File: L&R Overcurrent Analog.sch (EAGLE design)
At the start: 22 parts, among them IC1 CSLA2CFTH, IC2 TLC393CPN, IC3 7805TV, Q1 SUP75P0307, Q2 SUP75P0307, X1 J1

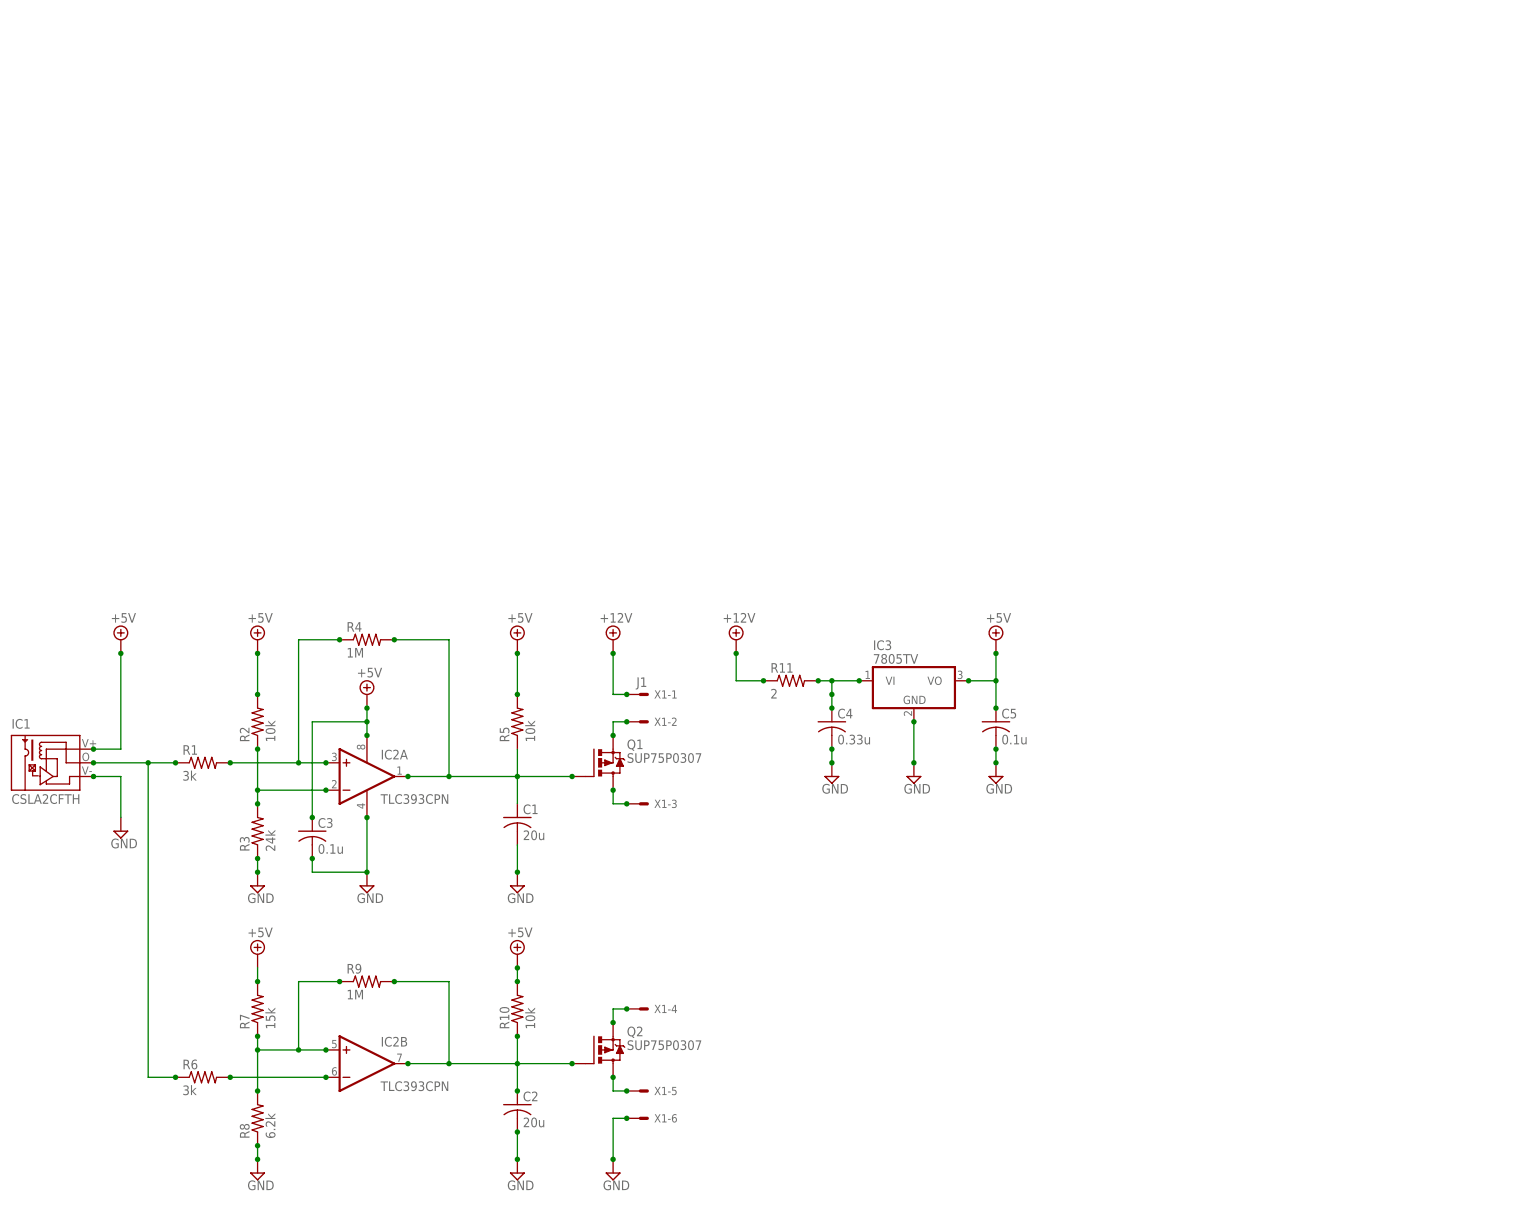
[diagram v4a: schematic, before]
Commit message: Split transducer from main board, added schematic frame.
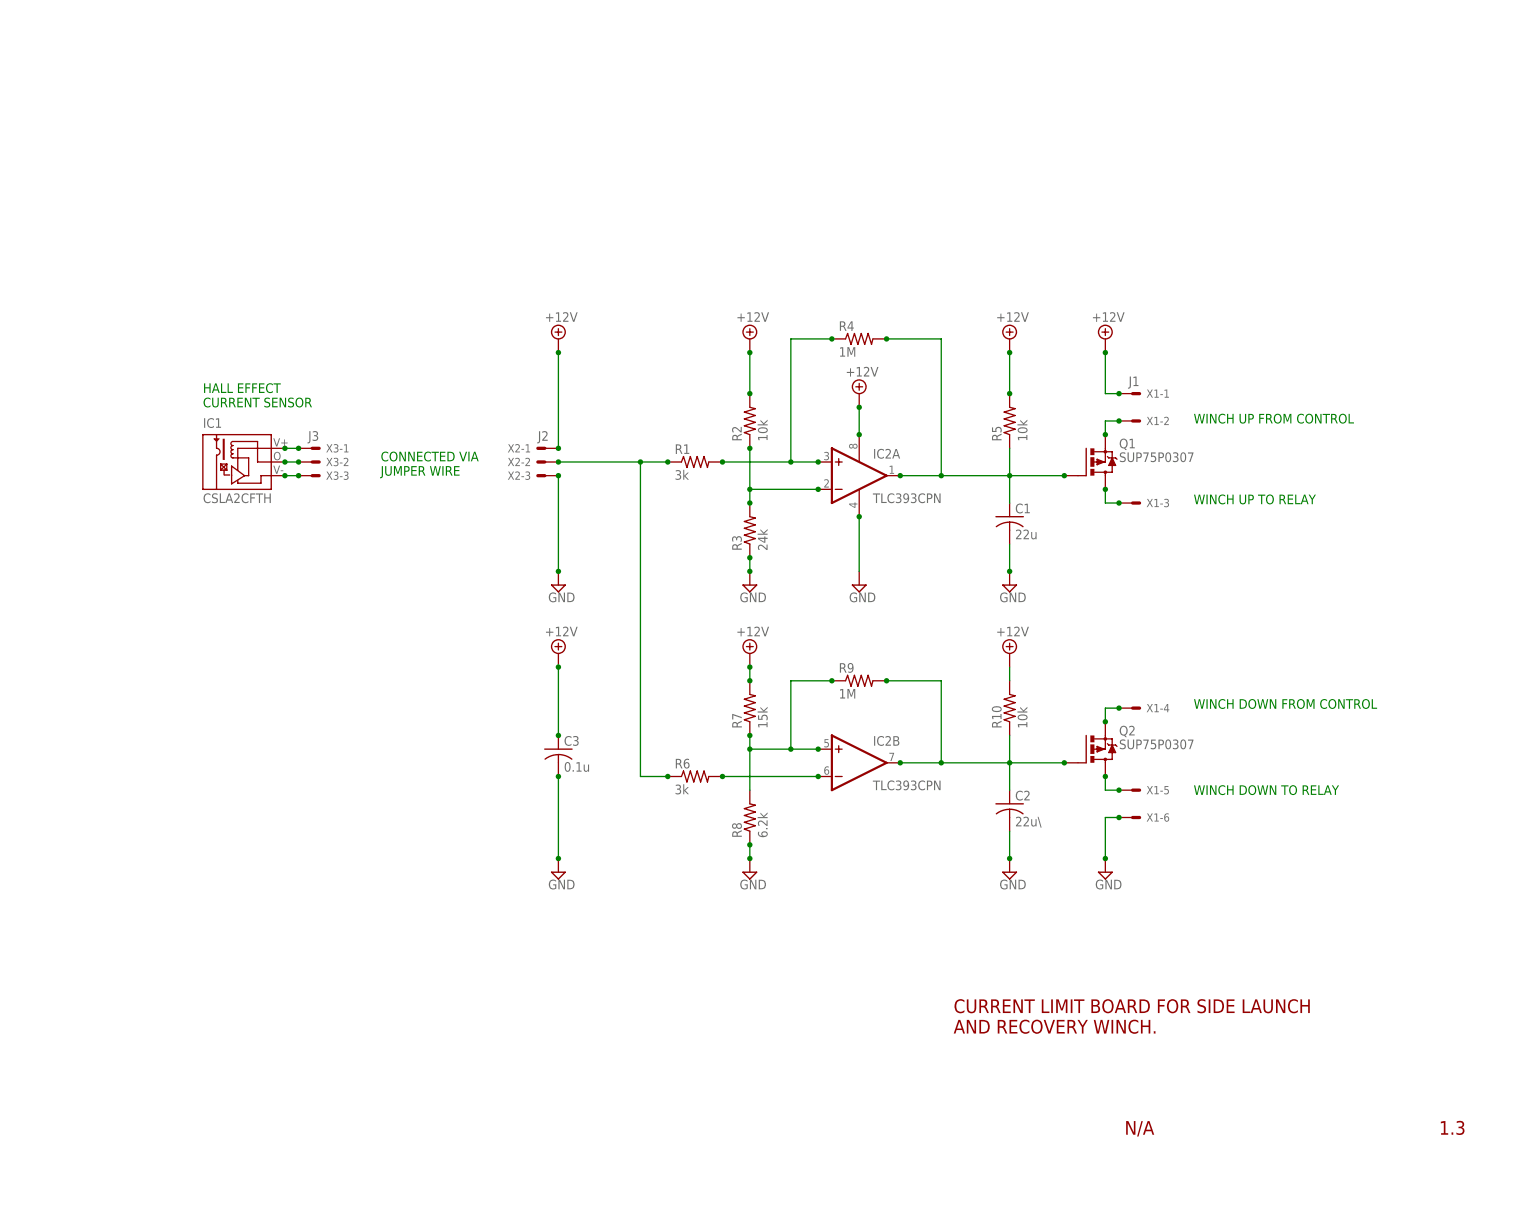
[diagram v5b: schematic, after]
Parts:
- removed C4: 0.33u, Overcurrent Detect:CAPACITOR-US
- removed C5: 0.1u, Overcurrent Detect:CAPACITOR-US
- removed IC3: 7805TV, Overcurrent Detect:7805TV
- removed R11: 2, Overcurrent Detect:RESISTOR-US0617/22
- added X2: J2, Overcurrent Detect:22-23-2031
- added X3: J3, Overcurrent Detect:22-23-2031
- C1: value 20u -> 22u
- C2: value 20u -> 22u\
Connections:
- removed net +5V: C3.1, C5.1, IC1.V+, IC2P.V+, IC3.VO, R10.2, R2.2, R5.2, R7.2
- removed net N$3: IC1.M, R1.1, R6.1
- new net N$13: IC1.V-, X3-3.S
- new net N$14: IC1.M, X3-2.S
- new net N$15: R1.1, R6.1, X2-2.S
- net +12V: now also C3.1, IC2P.V+, R10.2, R2.2, R5.2, R7.2, X2-1.S; no longer R11.1
- net GND: now also X2-3.S; no longer C4.2, C5.2, IC1.V-, IC3.GND
- net N$12: now also IC1.V+, X3-1.S; no longer C4.1, IC3.VI, R11.2
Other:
- note added: "1.3"
- note added: "CONNECTED VIA JUMPER WIRE"
- note added: "CURRENT LIMIT BOARD FOR SIDE LAUNCH AND RECOVERY WINCH."
- note added: "HALL EFFECT CURRENT SENSOR"
- note added: "N/A"
- note added: "WINCH DOWN FROM CONTROL"
- note added: "WINCH DOWN TO RELAY"
- note added: "WINCH UP FROM CONTROL"
- note added: "WINCH UP TO RELAY"
- moved on the sheet: C1, C2, C3, IC1, IC2A, IC2B, Q1, Q2, R1, R10, R2, R3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

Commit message: Updated / added document frames and added cutout to PCB
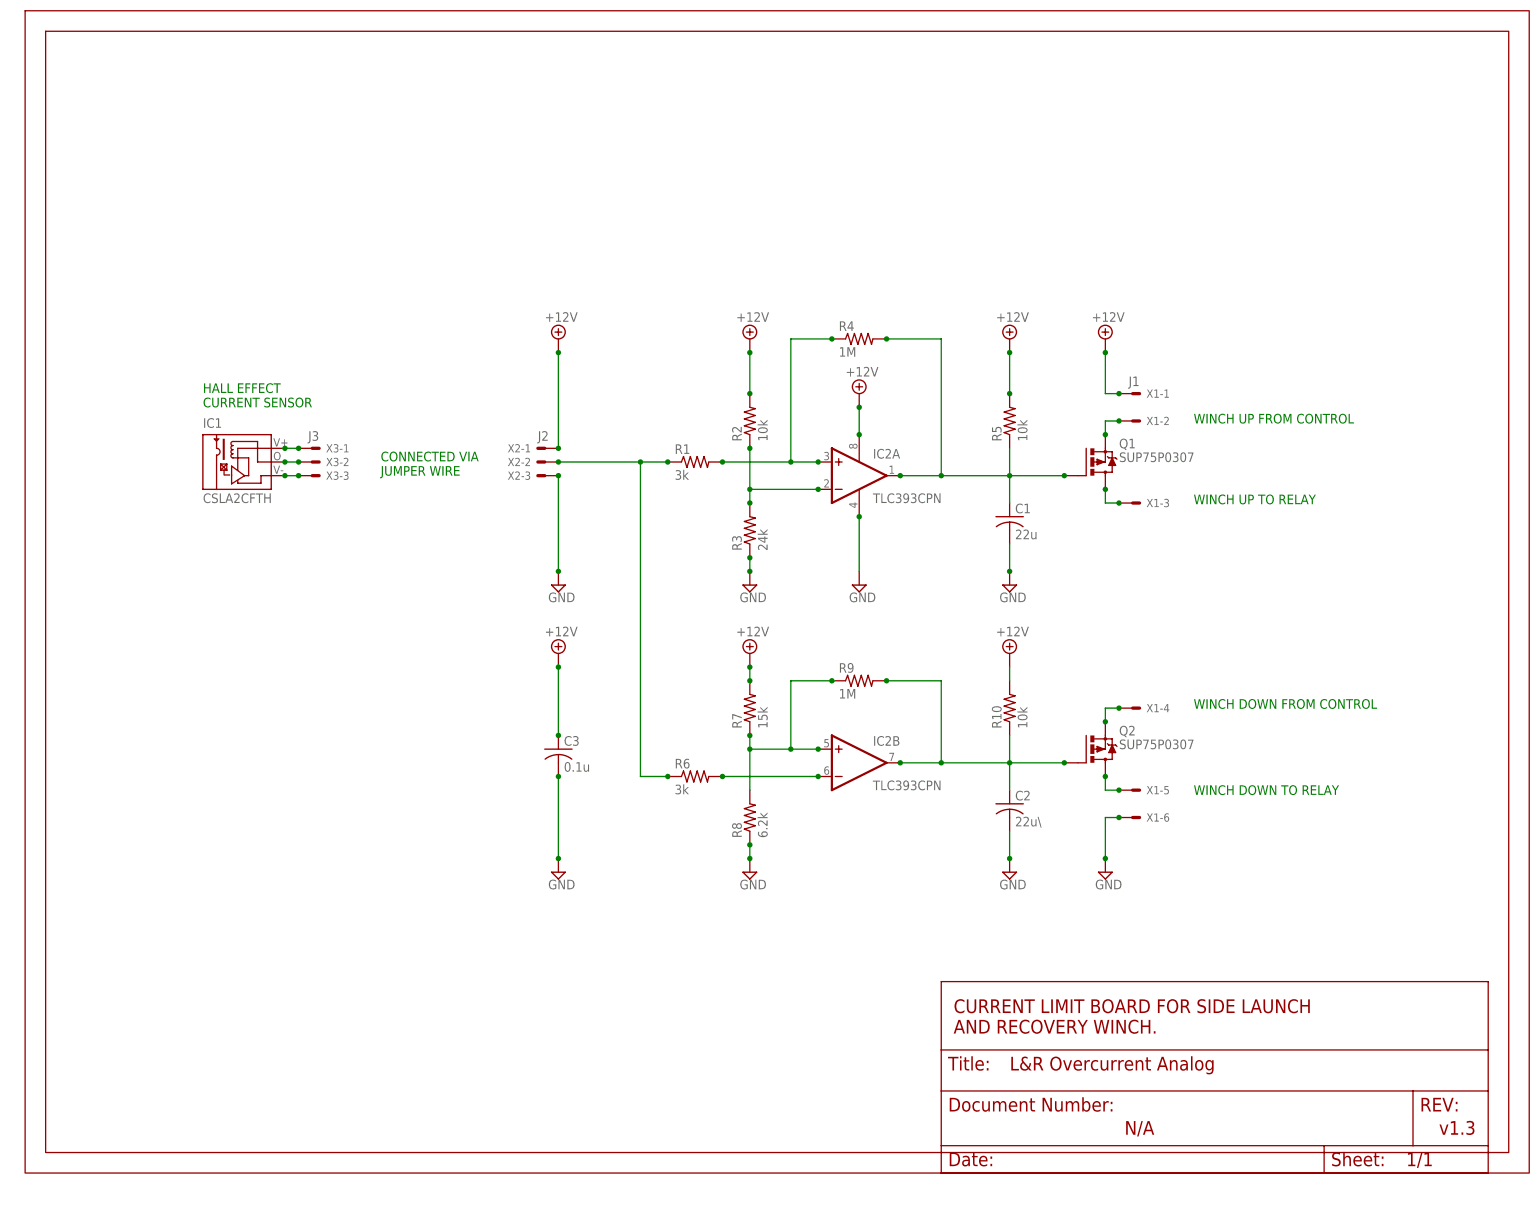
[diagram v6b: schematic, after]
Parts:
- added FRAME1: (no value), L&R Overcurrent Analog:FRAME_A_L
- added U$1: DOCFIELD, L&R Overcurrent Analog:DOCFIELD
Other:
- note added: "v1.3"
- note removed: "1.3"
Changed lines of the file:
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@@
 <setting verticaltext="up"/>
 </settings>
-<grid distance="0.1" unitdist="inch" unit="inch" style="lines" multiple="1" display="no" altdistance="0.01" altunitdist="inch" altunit="inch"/>
+<grid distance="0.1" unitdist="inch" unit="inch" style="lines" multiple="1" display="yes" altdistance="0.01" altunitdist="inch" altunit="inch"/>
 <layers>
 <layer number="1" name="Top" color="4" fill="1" visible="no" active="no"/>
+<layer number="2" name="Route2" color="1" fill="3" visible="no" active="no"/>
+<layer number="3" name="Route3" color="4" fill="3" visible="no" active="no"/>
+<layer number="4" name="Route4" color="1" fill="4" visible="no" active="no"/>
+<layer number="5" name="Route5" color="4" fill="4" visible="no" active="no"/>
+<layer number="6" name="Route6" color="1" fill="8" visible="no" active="no"/>
+<layer number="7" name="Route7" color="4" fill="8" visible="no" active="no"/>
+<layer number="8" name="Route8" color="1" fill="2" visible="no" active="no"/>
+<layer number="9" name="Route9" color="4" fill="2" visible="no" active="no"/>
+<layer number="10" name="Route10" color="1" fill="7" visible="no" active="no"/>
+<layer number="11" name="Route11" color="4" fill="7" visible="no" active="no"/>
+<layer number="12" name="Route12" color="1" fill="5" visible="no" active="no"/>
+<layer number="13" name="Route13" color="4" fill="5" visible="no" active="no"/>
+<layer number="14" name="Route14" color="1" fill="6" visible="no" active="no"/>
+<layer number="15" name="Route15" color="4" fill="6" visible="no" active="no"/>
 <layer number="16" name="Bottom" color="1" fill="1" visible="no" active="no"/>
 <layer number="17" name="Pads" color="2" fill="1" visible="no" active="no"/>
@@
 <layer number="48" name="Document" color="7" fill="1" visible="no" active="no"/>
 <layer number="49" name="Reference" color="7" fill="1" visible="no" active="no"/>
+<layer number="50" name="dxf" color="7" fill="1" visible="no" active="no"/>
 <layer number="51" name="tDocu" color="6" fill="1" visible="no" active="no"/>
 <layer number="52" name="bDocu" color="7" fill="1" visible="no" active="no"/>
+<layer number="53" name="tGND_GNDA" color="7" fill="9" visible="no" active="no"/>
+<layer number="54" name="bGND_GNDA" color="1" fill="9" visible="no" active="no"/>
+<layer number="56" name="wert" color="7" fill="1" visible="no" active="no"/>
 <layer number="91" name="Nets" color="2" fill="1" visible="yes" active="yes"/>
 <layer number="92" name="Busses" color="1" fill="1" visible="yes" active="yes"/>
@@
 <layer number="97" name="Info" color="7" fill="1" visible="yes" active="yes"/>
 <layer number="98" name="Guide" color="6" fill="1" visible="yes" active="yes"/>
+<layer number="100" name="Muster" color="7" fill="1" visible="yes" active="yes"/>
+<layer number="101" name="Flex-Kleb" color="1" fill="7" visible="yes" active="yes"/>
+<layer number="102" name="fp2" color="7" fill="1" visible="yes" active="yes"/>
+<layer number="103" name="fp3" color="7" fill="1" visible="yes" active="yes"/>
+<layer number="104" name="fp4" color="7" fill="1" visible="yes" active="yes"/>
+<layer number="105" name="Beschreib" color="9" fill="1" visible="yes" active="yes"/>
+<layer number="106" name="BGA-Top" color="4" fill="1" visible="yes" active="yes"/>
+<layer number="107" name="BD-Top" color="5" fill="1" visible="yes" active="yes"/>
+<layer number="108" name="fp8" color="7" fill="1" visible="yes" active="yes"/>
+<layer number="109" name="fp9" color="7" fill="1" visible="yes" active="yes"/>
+<layer number="110" name="fp0" color="7" fill="1" visible="yes" active="yes"/>
+<layer number="111" name="LPC17xx" color="7" fill="1" visible="yes" active="yes"/>
+<layer number="112" name="tSilk" color="7" fill="1" visible="yes" active="yes"/>
+<layer number="116" name="Patch_BOT" color="9" fill="4" visible="yes" active="yes"/>
+<layer number="121" name="tTestdril" color="7" fill="1" visible="yes" active="yes"/>
+<layer number="122" name="bTestdril" color="7" fill="1" visible="yes" active="yes"/>
+<layer number="123" name="tTestmark" color="7" fill="1" visible="yes" active="yes"/>
+<layer number="124" name="bTestmark" color="7" fill="1" visible="yes" active="yes"/>
+<layer number="125" name="_tNames" color="7" fill="1" visible="yes" active="yes"/>
+<layer number="126" name="_bNames" color="7" fill="1" visible="yes" active="yes"/>
+<layer number="127" name="_tValues" color="7" fill="1" visible="yes" active="yes"/>
+<layer number="128" name="_bValues" color="7" fill="1" visible="yes" active="yes"/>
+<layer number="131" name="tAdjust" color="7" fill="1" visible="yes" active="yes"/>
+<layer number="132" name="bAdjust" color="7" fill="1" visible="yes" active="yes"/>
+<layer number="144" name="Drill_legend" color="7" fill="1" visible="yes" active="yes"/>
+<layer number="151" name="HeatSink" color="7" fill="1" visible="yes" active="yes"/>
+<layer number="152" name="_bDocu" color="7" fill="1" visible="yes" active="yes"/>
+<layer number="199" name="Contour" color="7" fill="1" visible="yes" active="yes"/>
+<layer number="200" name="200bmp" color="7" fill="1" visible="yes" active="yes"/>
+<layer number="201" name="201bmp" color="7" fill="1" visible="yes" active="yes"/>
+<layer number="202" name="202bmp" color="7" fill="1" visible="yes" active="yes"/>
+<layer number="203" name="203bmp" color="7" fill="1" visible="yes" active="yes"/>
+<layer number="204" name="204bmp" color="7" fill="1" visible="yes" active="yes"/>
+<layer number="205" name="205bmp" color="7" fill="1" visible="yes" active="yes"/>
+<layer number="206" name="206bmp" color="7" fill="1" visible="yes" active="yes"/>
+<layer number="207" name="207bmp" color="7" fill="1" visible="yes" active="yes"/>
+<layer number="208" name="208bmp" color="7" fill="1" visible="yes" active="yes"/>
+<layer number="209" name="209bmp" color="7" fill="1" visible="yes" active="yes"/>
+<layer number="210" name="210bmp" color="7" fill="1" visible="yes" active="yes"/>
+<layer number="211" name="211bmp" color="7" fill="1" visible="yes" active="yes"/>
+<layer number="212" name="212bmp" color="7" fill="1" visible="yes" active="yes"/>
+<layer number="213" name="213bmp" color="7" fill="1" visible="yes" active="yes"/>
+<layer number="214" name="214bmp" color="7" fill="1" visible="yes" active="yes"/>
+<layer number="215" name="215bmp" color="7" fill="1" visible="yes" active="yes"/>
+<layer number="216" name="216bmp" color="7" fill="1" visible="yes" active="yes"/>
+<layer number="217" name="217bmp" color="18" fill="1" visible="no" active="no"/>
+<layer number="218" name="218bmp" color="19" fill="1" visible="no" active="no"/>
+<layer number="219" name="219bmp" color="20" fill="1" visible="no" active="no"/>
+<layer number="220" name="220bmp" color="21" fill="1" visible="no" active="no"/>
+<layer number="221" name="221bmp" color="22" fill="1" visible="no" active="no"/>
+<layer number="222" name="222bmp" color="23" fill="1" visible="no" active="no"/>
+<layer number="223" name="223bmp" color="24" fill="1" visible="no" active="no"/>
+<layer number="224" name="224bmp" color="25" fill="1" visible="no" active="no"/>
+<layer number="248" name="Housing" color="7" fill="1" visible="yes" active="yes"/>
+<layer number="249" name="Edge" color="7" fill="1" visible="yes" active="yes"/>
+<layer number="250" name="Descript" color="3" fill="1" visible="no" active="no"/>
+<layer number="251" name="SMDround" color="12" fill="11" visible="no" active="no"/>
+<layer number="254" name="OrgLBR" color="7" fill="1" visible="yes" active="yes"/>
 </layers>
 <schematic xreflabel="%F%N/%S.%C%R" xrefpart="/%S.%C%R">
@@
 <part name="X2" library="Overcurrent Detect" deviceset="22-23-2031" device="" value="J2"/>
 <part name="X3" library="Overcurrent Detect" deviceset="22-23-2031" device="" value="J3"/>
-<part name="FRAME1" library="Overcurrent Detect" deviceset="FRAME_A_L" device=""/>
 <part name="SUPPLY15" library="Overcurrent Detect" deviceset="+12V" device=""/>
 <part name="SUPPLY16" library="Overcurrent Detect" deviceset="GND" device=""/>
+<part name="FRAME1" library="L&amp;R Overcurrent Analog" deviceset="FRAME_A_L" device=""/>
+<part name="U$1" library="L&amp;R Overcurrent Analog" deviceset="DOCFIELD" device=""/>
 </parts>
 <sheets>
@@
 <text x="-66.04" y="93.98" size="1.778" layer="91">HALL EFFECT
 CURRENT SENSOR</text>
-<text x="163.576" y="-41.148" size="2.54" layer="94">1.3</text>
+<text x="163.576" y="-41.148" size="2.54" layer="94">v1.3</text>
 <text x="73.406" y="-22.352" size="2.54" layer="94">CURRENT LIMIT BOARD FOR SIDE LAUNCH
 AND RECOVERY WINCH.</text>
@@
 <instance part="X3" gate="-2" x="-45.72" y="83.82"/>
 <instance part="X3" gate="-3" x="-45.72" y="81.28"/>
-<instance part="FRAME1" gate="G$1" x="-101.6" y="-48.26"/>
-<instance part="FRAME1" gate="G$2" x="71.12" y="-48.26"/>
 <instance part="SUPPLY15" gate="+12V" x="0" y="48.26"/>
 <instance part="SUPPLY16" gate="GND" x="0" y="7.62"/>
+<instance part="FRAME1" gate="G$1" x="-99.06" y="-48.26"/>
+<instance part="U$1" gate="G$1" x="71.12" y="-48.26"/>
 </instances>
 <busses>

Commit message: Minor updates to silkscreen, added cutout to PCB
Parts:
- IC1: value CSLA2CFTH -> TLC393CPN; device Overcurrent Detect:CSLA2CFTH -> Overcurrent Detect:TLC393CPN
- IC2: value TLC393CPN -> CSLA2CFTH; device Overcurrent Detect:TLC393CPN -> Overcurrent Detect:CSLA2CFTH
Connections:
- net +12V: now also IC1P.V+; no longer IC2P.V+
- net GND: now also IC1P.V-; no longer IC2P.V-
- net N$1: now also IC1A.+IN; no longer IC2A.+IN
- net N$12: now also IC2.V+; no longer IC1.V+
- net N$13: now also IC2.V-; no longer IC1.V-
- net N$14: now also IC2.M; no longer IC1.M
- net N$2: now also IC1A.-IN; no longer IC2A.-IN
- net N$4: now also IC1B.-IN; no longer IC2B.-IN
- net N$5: now also IC1B.+IN; no longer IC2B.+IN
- net N$6: now also IC1A.OUT; no longer IC2A.OUT
- net N$7: now also IC1B.OUT; no longer IC2B.OUT
